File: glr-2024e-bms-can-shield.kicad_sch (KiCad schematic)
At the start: 13 parts, among them CN10 Conn_02x19_Odd_Even_MountingP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, CN7 Conn_02x19_Odd_Even_MountingP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, IC1 TLE6250GV33XUMA1, IC2 L9615D013TR, J1 Screw_Terminal_01x08

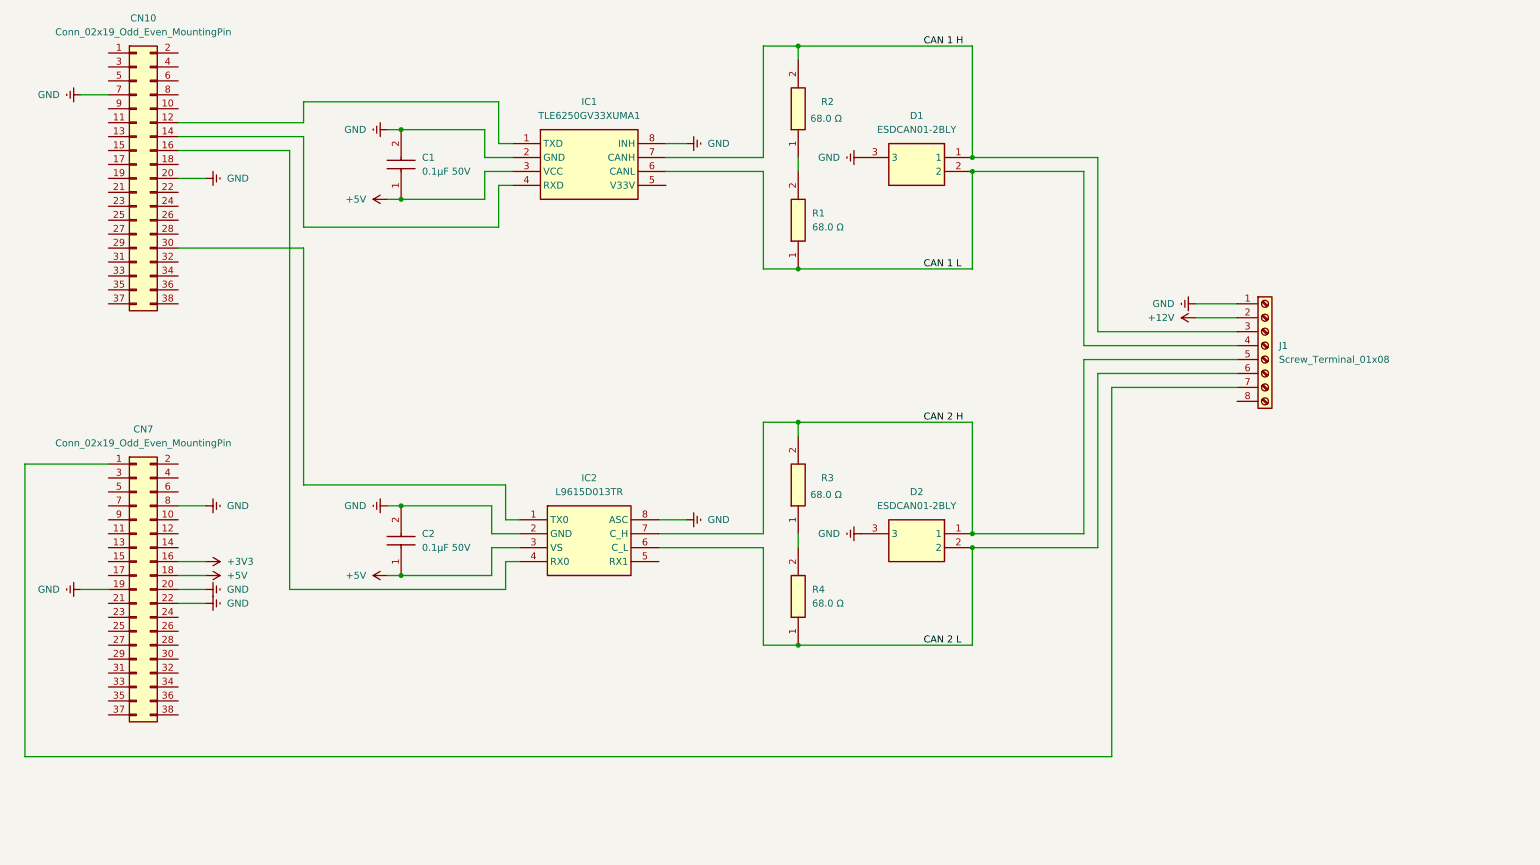
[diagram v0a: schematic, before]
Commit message: add  relay and optocopler
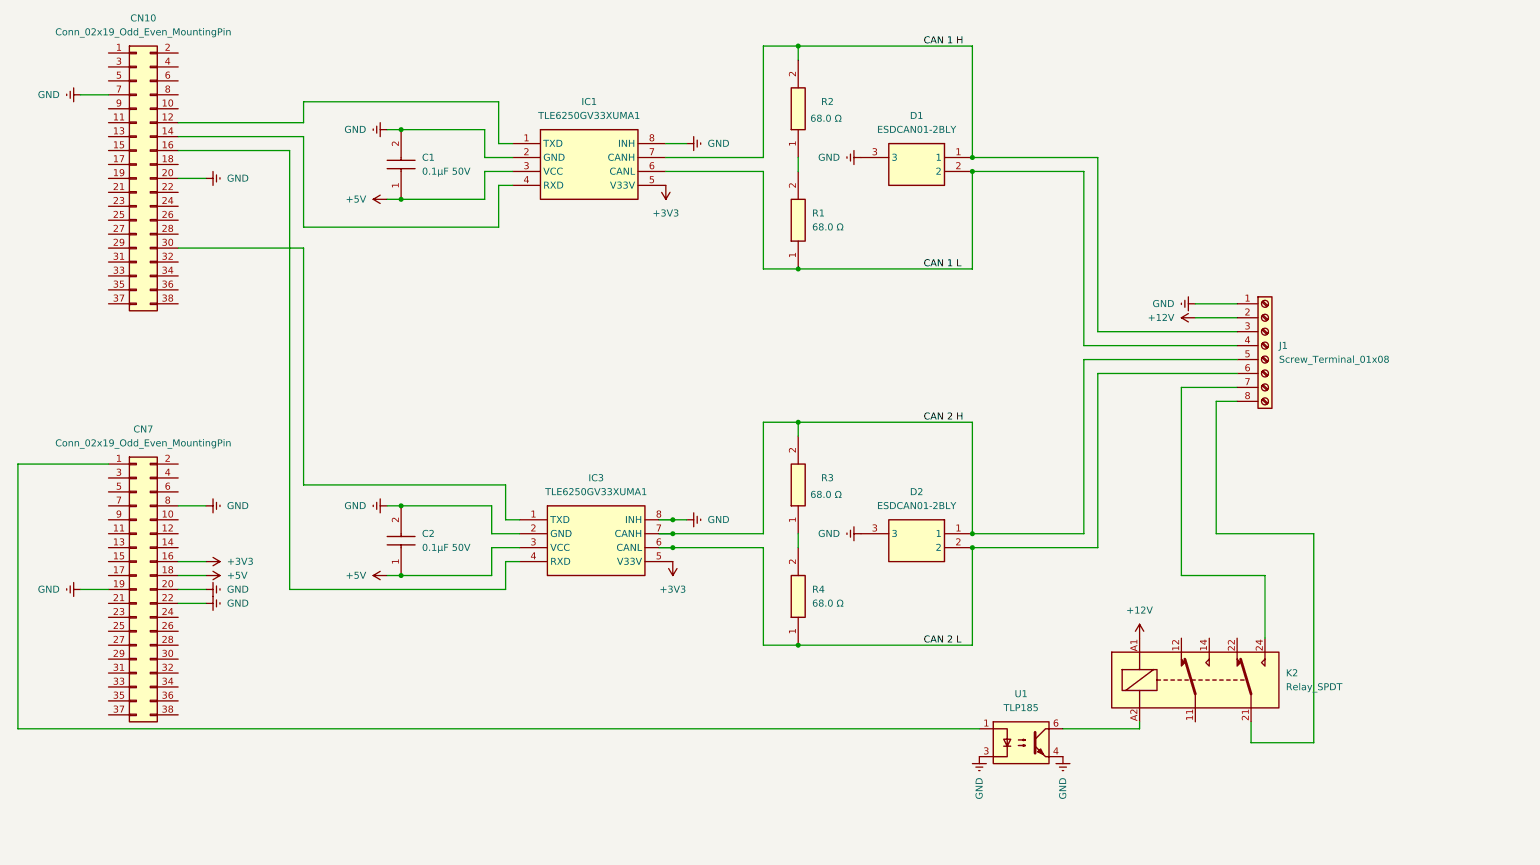
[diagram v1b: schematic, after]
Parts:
- removed IC2: L9615D013TR, SOIC127P600X175-8N, symbol SamacSys_Parts:L9615D013TR
- added IC3: TLE6250GV33XUMA1, SOIC127P600X175-8N, symbol SamacSys_Parts:TLE6250GV33XUMA1
- added K2: Relay_SPDT, symbol Relay:Relay_DPDT
- added U1: TLP185, Package_SO:SOIC-4_4.55x3.7mm_P2.54mm, symbol Isolator:TLP185
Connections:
- net +12V: now also K2.A1
- net +3V3: now also IC1.5 (V33V), IC3.5 (V33V)
- net +5V: now also IC3.3 (VCC)
- net CAN 2 H: now also IC3.7 (CANH)
- net CAN 2 L: now also IC3.6 (CANL)
- net GND: now also IC3.2 (GND), IC3.8 (INH), U1.3, U1.4
- net at CN10.16 (Pin_16): now also IC3.4 (RXD)
- net at CN10.30 (Pin_30): now also IC3.1 (TXD)
- net at J1.7 (Pin_7): now also K2.24; no longer CN7.1 (Pin_1)
- net at J1.8 (Pin_8): now also K2.21
- new net: K2.A2, U1.6
- new net: CN7.1 (Pin_1), U1.1

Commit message: the last touch
I added two transistors. The first one replaces the optocoupler and controls the relay: when 3.3 V is present at the input (which indicates a fault), the transistor switches on and activates the relay. If no voltage is present, the relay remains off.

The second transistor is used to turn the charger on and off. For this purpose, it was necessary to connect 12 V to its collector.
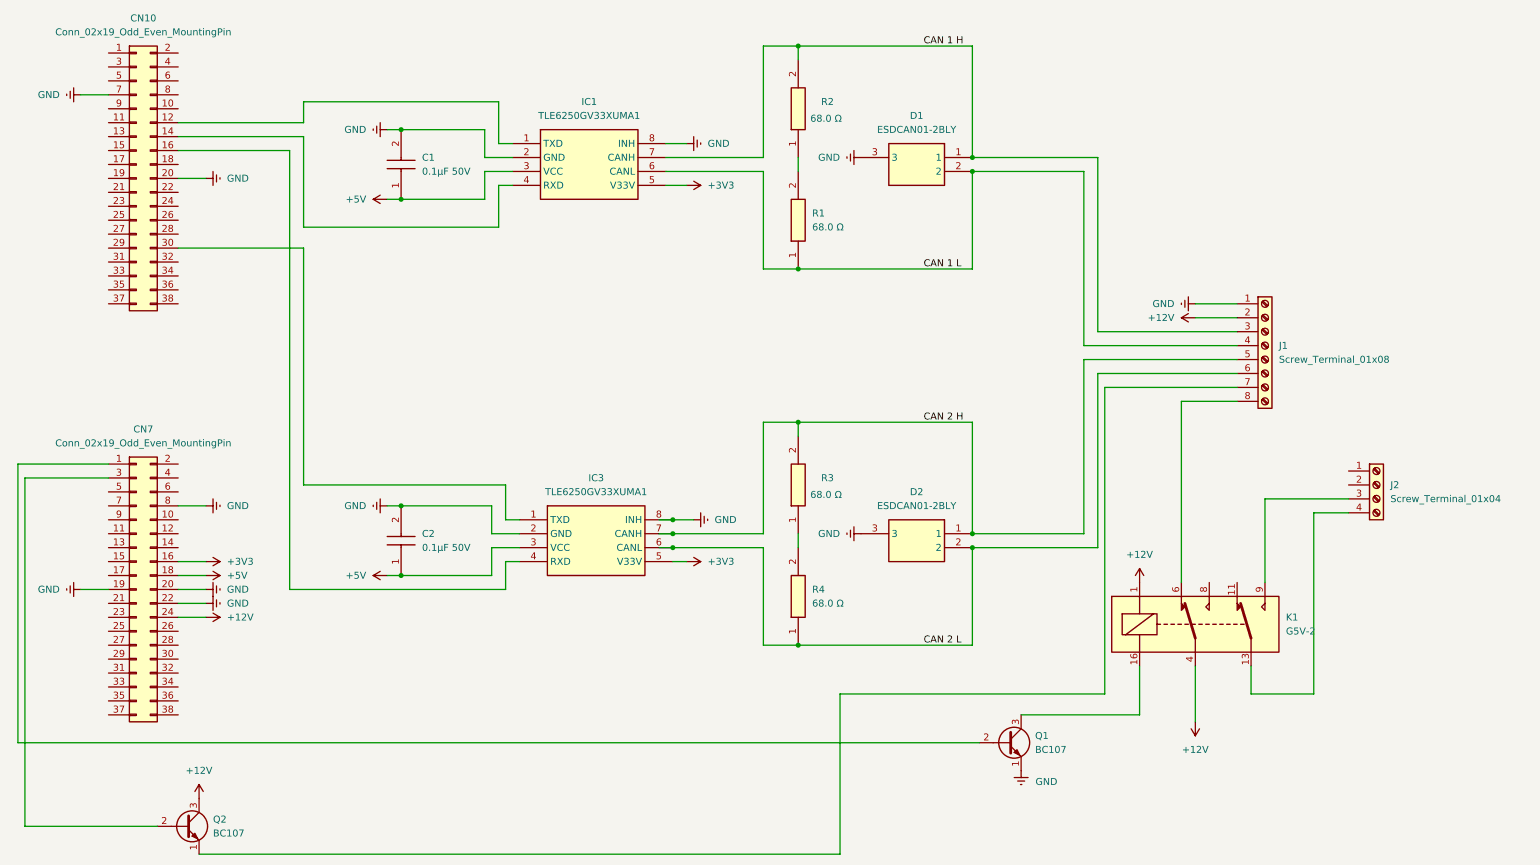
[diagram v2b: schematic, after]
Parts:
- removed K2: Relay_SPDT, symbol Relay:Relay_DPDT
- removed U1: TLP185, Package_SO:SOIC-4_4.55x3.7mm_P2.54mm, symbol Isolator:TLP185
- added J2: Screw_Terminal_01x04, GLR_KiCAD_Library:WECO-950-FB-04, symbol Connector:Screw_Terminal_01x04
- added K1: G5V-2, Relay_THT:Relay_DPDT_Omron_G5V-2, symbol Relay:G5V-2
- added Q1, Q2: BC107, Package_TO_SOT_SMD:SOT-23, symbol Transistor_BJT:BC107
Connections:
- net +12V: now also CN7.24 (Pin_24), K1.1, K1.4, Q2.3 (C)
- net GND: now also Q1.1 (E)
- net at J1.8 (Pin_8): now also K1.6
- net at J1.7 (Pin_7): now also Q2.1 (E)
- net at CN7.1 (Pin_1): now also Q1.2 (B)
- net at CN7.3 (Pin_3): now also Q2.2 (B)
- new net: J2.3 (Pin_3), K1.9
- new net: J2.4 (Pin_4), K1.13
- new net: K1.16, Q1.3 (C)

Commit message: more details to understand
explaining how work the process between the socket and the transistors
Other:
- note added: "BMS-charger: 0V : Stop charging 3.3V : Start charging"
- note added: "BMS-fault: 0V : Error 3.3V : No error"
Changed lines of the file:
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@@
 		(comment 2 "Ahmed Bouzidi")
+	)
+	(text "BMS-charger:\n0V : Stop charging\n3.3V : Start charging"
+		(exclude_from_sim no)
+		(at 33.274 168.402 0)
+		(effects
+			(font
+				(size 1.27 1.27)
+			)
+		)
+	)
+	(text "BMS-fault:\n0V : Error\n3.3V : No error "
+		(exclude_from_sim no)
+		(at 97.028 153.162 0)
+		(effects
+			(font
+				(size 1.27 1.27)
+			)
+		)
 	)
 	(junction

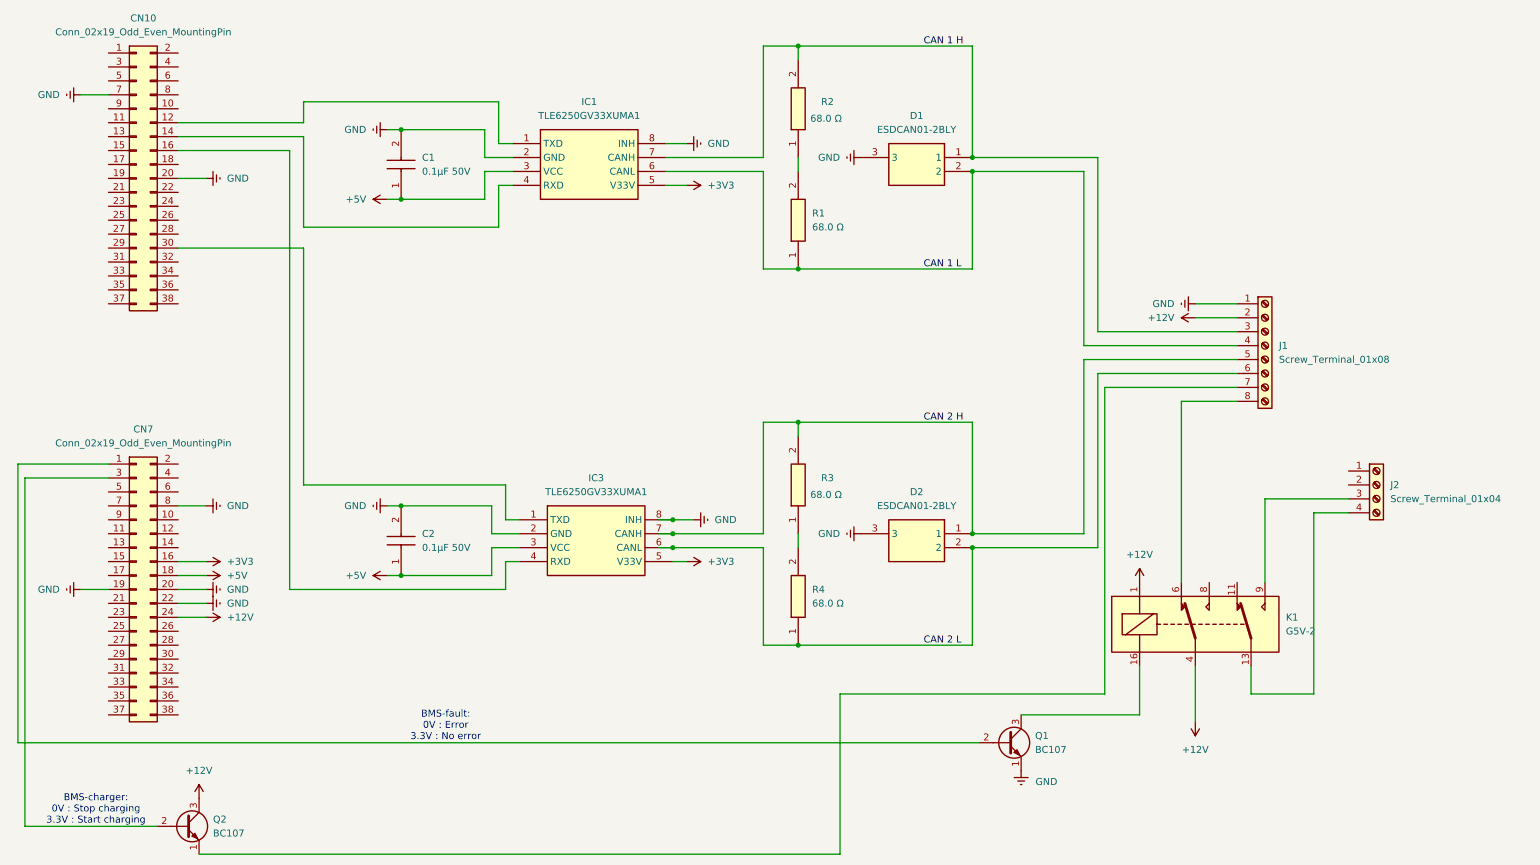
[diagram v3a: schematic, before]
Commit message: use Würth Elektronik TBL connectors
do some restructuring
add project specific libraries
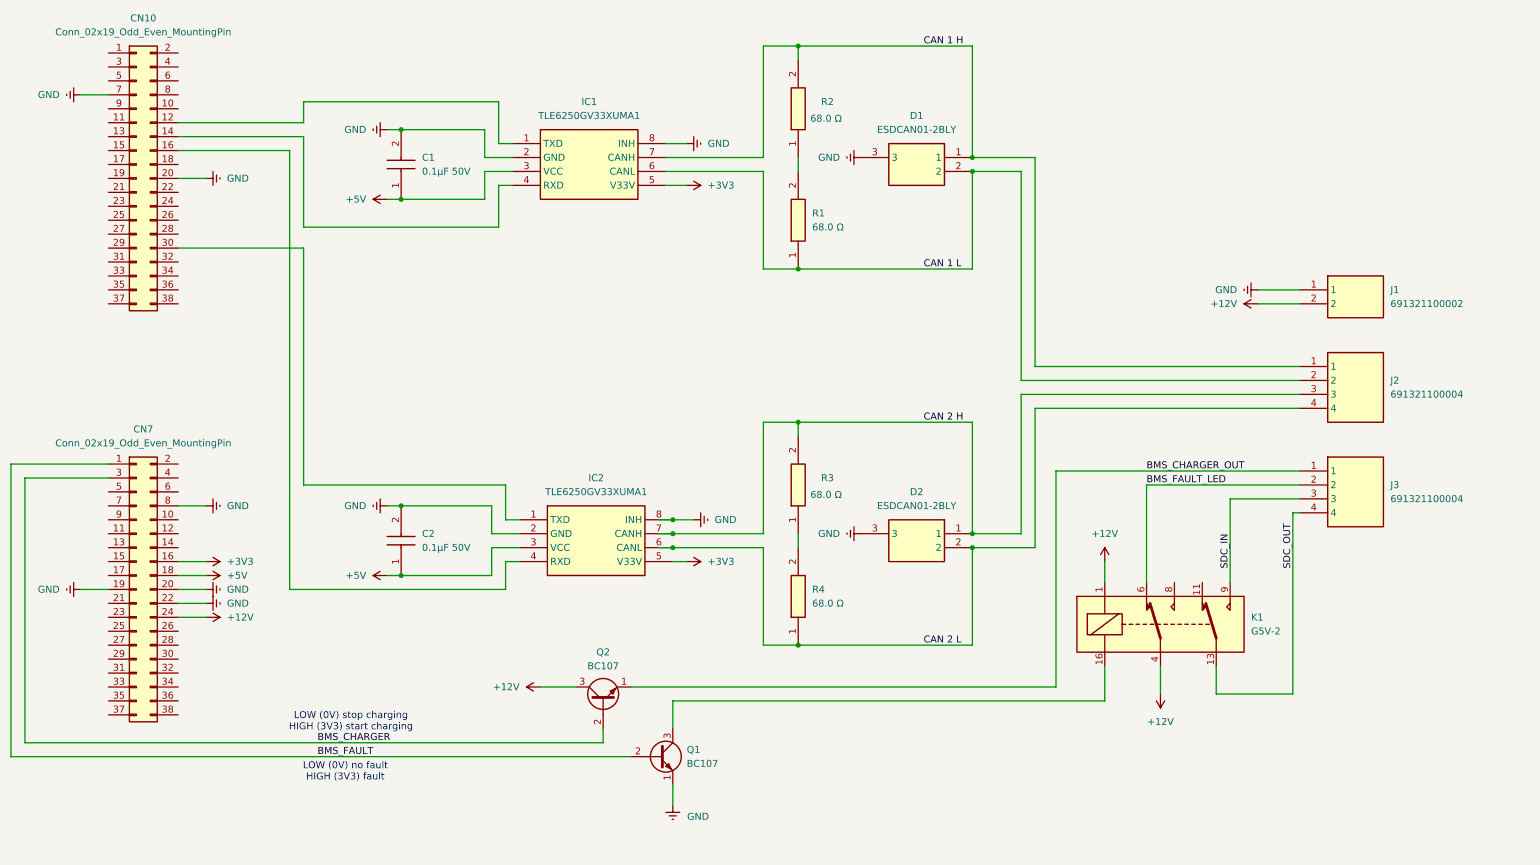
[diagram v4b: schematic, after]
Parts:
- removed J1: Screw_Terminal_01x08, GLR_KiCad_Library:WECO-950-FB-08, symbol Connector:Screw_Terminal_01x08
- removed J2: Screw_Terminal_01x04, GLR_KiCAD_Library:WECO-950-FB-04, symbol Connector:Screw_Terminal_01x04
- added J1: 691321100002, SamacSys_Parts:691321100002, symbol SamacSys_Parts:691321100002
- added J2, J3: 691321100004, 691321100004, symbol SamacSys_Parts:691321100004
- renumbered IC3 to IC2
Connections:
- net +12V: now also J1.2
- net CAN 1 H: now also J2.1
- net CAN 1 L: now also J2.2
- net CAN 2 H: now also J2.3
- net CAN 2 L: now also J2.4
- net GND: now also J1.1
- net SDC_IN: now reaches K1.9
- net SDC_IN: now also J3.3
- net SDC_OUT: now reaches K1.13
- net SDC_OUT: now also J3.4
- net BMS_CHARGER_OUT: now reaches Q2.1 (E)
- net BMS_CHARGER_OUT: now also J3.1
- net BMS_CHARGER: now reaches CN7.3 (Pin_3), Q2.2 (B)
- net BMS_FAULT_LED: now reaches K1.6
- net BMS_FAULT_LED: now also J3.2
- net BMS_FAULT: now reaches CN7.1 (Pin_1), Q1.2 (B)
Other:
- note added: "LOW (0V) no fault HIGH (3V3) fault"
- note added: "LOW (0V) stop charging HIGH (3V3) start charging"
- note removed: "BMS-charger: 0V : Stop charging 3.3V : Start charging"
- note removed: "BMS-fault: 0V : Error 3.3V : No error"
- moved on the sheet: K1, Q1, Q2

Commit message: update needed parts
not sure about these transistors
add pdf to ignore list

Co-Authored-By: wallalex0 <97884125+wallalex0@users.noreply.github.com>
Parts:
- Q1: value BC107 -> Q_NPN_EBC; footprint Package_TO_SOT_SMD:SOT-23 -> Package_TO_SOT_THT:TO-18-3; symbol Transistor_BJT:BC107 -> Transistor_BJT:Q_NPN_EBC
- Q2: value BC107 -> Q_NPN_EBC; symbol Transistor_BJT:BC107 -> Transistor_BJT:Q_NPN_EBC
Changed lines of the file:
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@@
 	)
 	(symbol
-		(lib_id "Transistor_BJT:BC107")
+		(lib_id "Transistor_BJT:Q_NPN_EBC")
 		(at 125.73 148.59 90)
 		(unit 1)
@@
 			)
 		)
-		(property "Value" "BC107"
+		(property "Value" "Q_NPN_EBC"
 			(at 125.73 142.24 90)
 			(effects
@@
 		)
 		(property "Footprint" "Package_TO_SOT_SMD:SOT-23"
-			(at 127.635 143.51 0)
-			(effects
-				(font
-					(size 1.27 1.27)
-					(italic yes)
-				)
-				(justify left)
-				(hide yes)
-			)
-		)
-		(property "Datasheet" "http://www.b-kainka.de/Daten/Transistor/BC108.pdf"
+			(at 123.19 143.51 0)
+			(effects
+				(font
+					(size 1.27 1.27)
+				)
+				(hide yes)
+			)
+		)
+		(property "Datasheet" "~"
 			(at 125.73 148.59 0)
 			(effects
@@
 					(size 1.27 1.27)
 				)
-				(justify left)
-				(hide yes)
-			)
-		)
-		(property "Description" "0.1A Ic, 50V Vce, Low Noise General Purpose NPN Transistor, TO-18"
+				(hide yes)
+			)
+		)
+		(property "Description" "NPN transistor, emitter/base/collector"
 			(at 125.73 148.59 0)
 			(effects
@@
 			)
 		)
+		(pin "1"
+		)
+		(pin "2"
+		)
 		(pin "3"
-		)
-		(pin "1"
-		)
-		(pin "2"
 		)
 		(instances
@@
 	)
 	(symbol
-		(lib_id "Transistor_BJT:BC107")
+		(lib_id "Transistor_BJT:Q_NPN_EBC")
 		(at 135.89 158.75 0)
 		(unit 1)
@@
 			)
 		)
-		(property "Value" "BC107"
+		(property "Value" "Q_NPN_EBC"
 			(at 140.97 160.0199 0)
 			(effects
@@
 			)
 		)
-		(property "Footprint" "Package_TO_SOT_SMD:SOT-23"
-			(at 140.97 160.655 0)
-			(effects
-				(font
-					(size 1.27 1.27)
-					(italic yes)
-				)
-				(justify left)
-				(hide yes)
-			)
-		)
-		(property "Datasheet" "http://www.b-kainka.de/Daten/Transistor/BC108.pdf"
+		(property "Footprint" "Package_TO_SOT_THT:TO-18-3"
+			(at 140.97 156.21 0)
+			(effects
+				(font
+					(size 1.27 1.27)
+				)
+				(hide yes)
+			)
+		)
+		(property "Datasheet" "~"
 			(at 135.89 158.75 0)
 			(effects
@@
 					(size 1.27 1.27)
 				)
-				(justify left)
-				(hide yes)
-			)
-		)
-		(property "Description" "0.1A Ic, 50V Vce, Low Noise General Purpose NPN Transistor, TO-18"
+				(hide yes)
+			)
+		)
+		(property "Description" "NPN transistor, emitter/base/collector"
 			(at 135.89 158.75 0)
 			(effects
@@
 			)
 		)
+		(pin "2"
+		)
 		(pin "3"
 		)
 		(pin "1"
 		)
-		(pin "2"
-		)
-		(instances
+		(instances
